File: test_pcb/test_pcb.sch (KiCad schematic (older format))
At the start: 19 parts, among them K0 KEYSW, K1 KEYSW, K2 KEYSW, K3 KEYSW, K5 KEYSW, U1 74HC595, U2 Teensy3.2

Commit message: updated test_pcb
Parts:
- added P1, P2: CONN_01X08, Pin_Headers:Pin_Header_Straight_1x08_Pitch2.00mm, symbol CONN_01X08
- added U2: 74HC595, Housings_SSOP:TSSOP-16_4.4x5mm_Pitch0.65mm, symbol 74HC595
- U0: renamed from U2; footprint Socket_Strips:Socket_Strip_Angled_2x27_Pitch2.54mm -> Teensy:Teensy30_31_32_LC
- U1: footprint SMD_Packages:SO-16-L -> Housings_SSOP:TSSOP-16_4.4x5mm_Pitch0.65mm
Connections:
- net labels added: GND, GND0, GND1, sr_clk0, sr_data0, sr_data1
- net labels removed: sr_data
- wire segments 46 -> 84
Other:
- moved on the sheet: D0, D1, D2, D3, D5, K0, K1, K2, K3, K5, U0

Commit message: test_pcb first pass complete
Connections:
- wire segments 84 -> 50
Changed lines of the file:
@@
 Text GLabel 8350 5050 0    60   Input ~ 0
 col1_sled_cath
+Text GLabel 8350 5750 0    60   Input ~ 0
+row0_sled_r
 Text GLabel 8350 5850 0    60   Input ~ 0
-row0_sled_r
+row0_sled_g
 Text GLabel 8350 5950 0    60   Input ~ 0
-row0_sled_g
+row0_sled_b
+Text GLabel 8350 6250 0    60   Input ~ 0
+row1_sled_r
+Text GLabel 8350 6150 0    60   Input ~ 0
+row1_sled_g
 Text GLabel 8350 6050 0    60   Input ~ 0
-row0_sled_b
-Text GLabel 8350 6150 0    60   Input ~ 0
-row1_sled_r
-Text GLabel 8350 6250 0    60   Input ~ 0
-row1_sled_g
-Text GLabel 8350 6350 0    60   Input ~ 0
 row1_sled_b
 Text GLabel 9750 5050 2    60   Input ~ 0
@@
 	4100 2150 4100 2200
 Wire Wire Line
-	2800 2400 3000 2400
-Wire Wire Line
-	3000 2400 4100 2400
-Wire Wire Line
-	4100 2400 5400 2400
-Wire Wire Line
-	2800 1900 3000 1900
-Wire Wire Line
-	3000 1900 4100 1900
+	2800 2400 5400 2400
+Wire Wire Line
+	2800 1900 4100 1900
 Connection ~ 3600 1650
 Connection ~ 4700 1650
@@
 Connection ~ 3000 2400
 Wire Wire Line
-	4800 3150 4800 3400
-Wire Wire Line
-	4800 3400 4800 3600
-Wire Wire Line
-	4800 3600 4800 3800
-Wire Wire Line
-	4800 3800 4800 4500
-Wire Wire Line
-	4800 4500 4800 4700
-Wire Wire Line
-	4800 4700 4800 4900
+	4800 3150 4800 4900
 Connection ~ 4800 4700
 Wire Wire Line
-	3000 3150 3000 3400
-Wire Wire Line
-	3000 3400 3000 3600
-Wire Wire Line
-	3000 3600 3000 3800
-Wire Wire Line
-	3000 3800 3000 4500
-Wire Wire Line
-	3000 4500 3000 4700
-Wire Wire Line
-	3000 4700 3000 4900
+	3000 3150 3000 4900
 Connection ~ 3000 4700
 Connection ~ 3000 3600
 Connection ~ 4800 3600
 Wire Wire Line
-	3600 4050 4500 4050
-Wire Wire Line
-	4500 4050 5400 4050
-Wire Wire Line
-	5400 4050 5500 4050
-Wire Wire Line
-	3500 4150 4400 4150
-Wire Wire Line
-	4400 4150 5300 4150
-Wire Wire Line
-	5300 4150 6100 4150
-Wire Wire Line
-	3400 4250 4300 4250
-Wire Wire Line
-	4300 4250 5200 4250
-Wire Wire Line
-	5200 4250 6100 4250
+	3600 4050 5500 4050
+Wire Wire Line
+	3500 4150 6100 4150
+Wire Wire Line
+	3400 4250 6100 4250
 Wire Wire Line
 	3400 3800 3400 4250
@@
 Connection ~ 5400 4050
 Wire Wire Line
-	3600 5150 4500 5150
-Wire Wire Line
-	4500 5150 5400 5150
-Wire Wire Line
-	5400 5150 5500 5150
-Wire Wire Line
-	3500 5250 4400 5250
-Wire Wire Line
-	4400 5250 5300 5250
-Wire Wire Line
-	5300 5250 6100 5250
-Wire Wire Line
-	3400 5350 4300 5350
-Wire Wire Line
-	4300 5350 5200 5350
-Wire Wire Line
-	5200 5350 6100 5350
+	3600 5150 5500 5150
+Wire Wire Line
+	3500 5250 6100 5250
+Wire Wire Line
+	3400 5350 6100 5350
 Wire Wire Line
 	5200 5350 5200 4900
@@
 Connection ~ 6000 1650
 Wire Wire Line
-	3900 3150 3900 3400
-Wire Wire Line
-	3900 3400 3900 3600
-Wire Wire Line
-	3900 3600 3900 3800
-Wire Wire Line
-	3900 3800 3900 4500
-Wire Wire Line
-	3900 4500 3900 4700
-Wire Wire Line
-	3900 4700 3900 4900
+	3900 3150 3900 4900
 Connection ~ 3900 4700
 Connection ~ 3900 3600
@@
 Connection ~ 6000 2150
 Wire Wire Line
-	6000 1650 6000 2150
-Wire Wire Line
-	6000 2150 6000 2500
-Wire Wire Line
-	4700 1650 4700 2150
-Wire Wire Line
-	4700 2150 4700 2500
-Wire Wire Line
-	3600 1650 3600 2150
-Wire Wire Line
-	3600 2150 3600 2500
+	6000 1650 6000 2500
+Wire Wire Line
+	4700 1650 4700 2500
+Wire Wire Line
+	3600 1650 3600 2500
 $Comp
 L 74HC595 U2
@@
 	10700 5850 10600 5850
 Wire Wire Line
-	10700 5650 10700 5750
-Wire Wire Line
-	10700 5750 10700 5850
+	10700 5650 10700 5850
 Wire Wire Line
 	10700 5650 10600 5650

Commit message: test_pcb small stuff
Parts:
- added P0: CONN_01X08, Connectors_Molex:Molex_PicoBlade_53261-0871_08x1.25mm_Angled, symbol CONN_01X08
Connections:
- net labels added: BTN0, BTN1, BTN2, DATA, TP_CLK, TP_RST, VCC
- net labels removed: GND0, GND1
- wire segments 50 -> 46
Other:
- moved on the sheet: D0, D1, D2, D3, D5, K0, K1, K2, K3, K5
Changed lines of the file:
@@
 L KEYSW K0
 U 1 1 5894086E
+P 3300 1150
+F 0 "K0" H 3250 1150 60  0000 C CNN
+F 1 "KEYSW" H 3300 1050 60  0001 C CNN
+F 2 "cherry_rgb:CHERRY_PLATE_NH_100H" H 3300 1150 60  0001 C CNN
+F 3 "" H 3300 1150 60  0000 C CNN
+	1    3300 1150
+	1    0    0    -1
+$EndComp
+$Comp
+L KEYSW K2
+U 1 1 58940BCD
+P 4400 1150
+F 0 "K2" H 4350 1150 60  0000 C CNN
+F 1 "KEYSW" H 4400 1050 60  0001 C CNN
+F 2 "cherry_rgb:CHERRY_PLATE_NH_100H" H 4400 1150 60  0001 C CNN
+F 3 "" H 4400 1150 60  0000 C CNN
+	1    4400 1150
+	1    0    0    -1
+$EndComp
+$Comp
+L KEYSW K1
+U 1 1 58940C88
 P 3300 1650
-F 0 "K0" H 3250 1650 60  0000 C CNN
+F 0 "K1" H 3250 1650 60  0000 C CNN
 F 1 "KEYSW" H 3300 1550 60  0001 C CNN
 F 2 "cherry_rgb:CHERRY_PLATE_NH_100H" H 3300 1650 60  0001 C CNN
@@
 $EndComp
 $Comp
-L KEYSW K2
-U 1 1 58940BCD
+L KEYSW K3
+U 1 1 58940C8E
 P 4400 1650
-F 0 "K2" H 4350 1650 60  0000 C CNN
+F 0 "K3" H 4350 1650 60  0000 C CNN
 F 1 "KEYSW" H 4400 1550 60  0001 C CNN
 F 2 "cherry_rgb:CHERRY_PLATE_NH_100H" H 4400 1650 60  0001 C CNN
@@
 $EndComp
 $Comp
-L KEYSW K1
-U 1 1 58940C88
-P 3300 2150
-F 0 "K1" H 3250 2150 60  0000 C CNN
-F 1 "KEYSW" H 3300 2050 60  0001 C CNN
-F 2 "cherry_rgb:CHERRY_PLATE_NH_100H" H 3300 2150 60  0001 C CNN
-F 3 "" H 3300 2150 60  0000 C CNN
-	1    3300 2150
-	1    0    0    -1
-$EndComp
-$Comp
-L KEYSW K3
-U 1 1 58940C8E
-P 4400 2150
-F 0 "K3" H 4350 2150 60  0000 C CNN
-F 1 "KEYSW" H 4400 2050 60  0001 C CNN
-F 2 "cherry_rgb:CHERRY_PLATE_NH_100H" H 4400 2150 60  0001 C CNN
-F 3 "" H 4400 2150 60  0000 C CNN
-	1    4400 2150
-	1    0    0    -1
-$EndComp
-$Comp
 L D D0
 U 1 1 58940C9B
+P 3000 1350
+F 0 "D0" V 2850 1300 60  0000 C CNN
+F 1 "D" V 3150 1300 60  0001 C CNN
+F 2 "Diodes_SMD:D_SOD-123" H 3000 1350 60  0001 C CNN
+F 3 "" H 3000 1350 60  0000 C CNN
+	1    3000 1350
+	-1   0    0    1
+$EndComp
+$Comp
+L D D2
+U 1 1 589410AE
+P 4100 1350
+F 0 "D2" V 3950 1300 60  0000 C CNN
+F 1 "D" V 4250 1300 60  0001 C CNN
+F 2 "Diodes_SMD:D_SOD-123" H 4100 1350 60  0001 C CNN
+F 3 "" H 4100 1350 60  0000 C CNN
+	1    4100 1350
+	-1   0    0    1
+$EndComp
+$Comp
+L D D1
+U 1 1 58941204
 P 3000 1850
-F 0 "D0" V 2850 1800 60  0000 C CNN
+F 0 "D1" V 2850 1800 60  0000 C CNN
 F 1 "D" V 3150 1800 60  0001 C CNN
 F 2 "Diodes_SMD:D_SOD-123" H 3000 1850 60  0001 C CNN
@@
 $EndComp
 $Comp
-L D D2
-U 1 1 589410AE
+L D D3
+U 1 1 5894120A
 P 4100 1850
-F 0 "D2" V 3950 1800 60  0000 C CNN
+F 0 "D3" V 3950 1800 60  0000 C CNN
 F 1 "D" V 4250 1800 60  0001 C CNN
 F 2 "Diodes_SMD:D_SOD-123" H 4100 1850 60  0001 C CNN
@@
 	-1   0    0    1
 $EndComp
-$Comp
-L D D1
-U 1 1 58941204
-P 3000 2350
-F 0 "D1" V 2850 2300 60  0000 C CNN
-F 1 "D" V 3150 2300 60  0001 C CNN
-F 2 "Diodes_SMD:D_SOD-123" H 3000 2350 60  0001 C CNN
-F 3 "" H 3000 2350 60  0000 C CNN
-	1    3000 2350
-	-1   0    0    1
-$EndComp
-$Comp
-L D D3
-U 1 1 5894120A
-P 4100 2350
-F 0 "D3" V 3950 2300 60  0000 C CNN
-F 1 "D" V 4250 2300 60  0001 C CNN
-F 2 "Diodes_SMD:D_SOD-123" H 4100 2350 60  0001 C CNN
-F 3 "" H 4100 2350 60  0000 C CNN
-	1    4100 2350
-	-1   0    0    1
-$EndComp
+Text GLabel 2800 1400 0    60   Input ~ 0
+row0
 Text GLabel 2800 1900 0    60   Input ~ 0
-row0
-Text GLabel 2800 2400 0    60   Input ~ 0
 row1
-Text GLabel 3600 2500 3    60   Input ~ 0
+Text GLabel 3600 2000 3    60   Input ~ 0
 col0
-Text GLabel 4700 2500 3    60   Input ~ 0
+Text GLabel 4700 2000 3    60   Input ~ 0
 col1
 Text GLabel 7000 2200 0    60   Input ~ 0
@@
 L KEYSW K5
 U 1 1 58950DFF
-P 5700 2150
-F 0 "K5" H 5650 2150 60  0000 C CNN
-F 1 "KEYSW" H 5700 2050 60  0001 C CNN
-F 2 "cherry_rgb:CHERRY_PLATE_NH_100H" H 5700 2150 60  0001 C CNN
-F 3 "" H 5700 2150 60  0000 C CNN
-	1    5700 2150
+P 5700 1650
+F 0 "K5" H 5650 1650 60  0000 C CNN
+F 1 "KEYSW" H 5700 1550 60  0001 C CNN
+F 2 "cherry_rgb:CHERRY_PLATE_NH_100H" H 5700 1650 60  0001 C CNN
+F 3 "" H 5700 1650 60  0000 C CNN
+	1    5700 1650
 	1    0    0    -1
 $EndComp
@@
 L D D5
 U 1 1 58950E0B
-P 5400 2350
-F 0 "D5" V 5250 2300 60  0000 C CNN
-F 1 "D" V 5550 2300 60  0001 C CNN
-F 2 "Diodes_SMD:D_SOD-123" H 5400 2350 60  0001 C CNN
-F 3 "" H 5400 2350 60  0000 C CNN
-	1    5400 2350
-	-1   0    0    1
-$EndComp
-Text GLabel 6000 2500 3    60   Input ~ 0
+P 5400 1850
+F 0 "D5" V 5250 1800 60  0000 C CNN
+F 1 "D" V 5550 1800 60  0001 C CNN
+F 2 "Diodes_SMD:D_SOD-123" H 5400 1850 60  0001 C CNN
+F 3 "" H 5400 1850 60  0000 C CNN
+	1    5400 1850
+	-1   0    0    1
+$EndComp
+Text GLabel 6000 2000 3    60   Input ~ 0
 col2
 $Comp
@@
 	1    0    0    -1
 $EndComp
+$Comp
+L 74HC595 U2
+U 1 1 58957349
+P 9050 5900
+F 0 "U2" H 9200 6500 50  0000 C CNN
+F 1 "74HC595" H 9050 5300 50  0000 C CNN
+F 2 "Housings_SSOP:TSSOP-16_4.4x5mm_Pitch0.65mm" H 9050 5900 50  0001 C CNN
+F 3 "" H 9050 5900 50  0000 C CNN
+	1    9050 5900
+	-1   0    0    1
+$EndComp
+Text GLabel 9750 6350 2    60   Input ~ 0
+sr_data1
+Text GLabel 10650 5300 0    60   Input ~ 0
+sr_data1
+$Comp
+L CONN_01X08 P1
+U 1 1 58957DB2
+P 10850 4950
+F 0 "P1" H 10850 5400 50  0000 C CNN
+F 1 "CONN_01X08" V 10950 4950 50  0000 C CNN
+F 2 "Pin_Headers:Pin_Header_Straight_1x08_Pitch2.00mm" H 10850 4950 50  0001 C CNN
+F 3 "" H 10850 4950 50  0000 C CNN
+	1    10850 4950
+	1    0    0    -1
+$EndComp
+Text GLabel 10650 4600 0    60   Input ~ 0
+sr_clk0
+Text GLabel 9750 4850 2    60   Input ~ 0
+sr_clk0
+Text GLabel 9750 6150 2    60   Input ~ 0
+sr_clk0
+Text GLabel 10650 4900 0    60   Input ~ 0
+GND
+Text GLabel 9750 4450 2    60   Input ~ 0
+GND
+Text GLabel 9750 5750 2    60   Input ~ 0
+GND
+Text GLabel 10650 5000 0    60   Input ~ 0
+VCC
+$Comp
+L CONN_01X08 P0
+U 1 1 5897F60A
+P 7600 3600
+F 0 "P0" H 7600 4050 50  0000 C CNN
+F 1 "CONN_01X08" V 7700 3600 50  0000 C CNN
+F 2 "Connectors_Molex:Molex_PicoBlade_53261-0871_08x1.25mm_Angled" H 7600 3600 50  0001 C CNN
+F 3 "" H 7600 3600 50  0000 C CNN
+	1    7600 3600
+	1    0    0    -1
+$EndComp
+Text GLabel 7400 3950 0    60   Input ~ 0
+BTN0
+Text GLabel 7400 3850 0    60   Input ~ 0
+BTN1
+Text GLabel 7400 3750 0    60   Input ~ 0
+BTN2
+Text GLabel 7400 3650 0    60   Input ~ 0
+VCC
+Text GLabel 7400 3250 0    60   Input ~ 0
+GND
+Text GLabel 7400 3350 0    60   Input ~ 0
+DATA
+Text GLabel 7400 3550 0    60   Input ~ 0
+TP_RST
+Text GLabel 7400 3450 0    60   Input ~ 0
+TP_CLK
+Wire Wire Line
+	3000 1150 3000 1200
+Wire Wire Line
+	4100 1150 4100 1200
 Wire Wire Line
 	3000 1650 3000 1700
@@
 	4100 1650 4100 1700
 Wire Wire Line
-	3000 2150 3000 2200
-Wire Wire Line
-	4100 2150 4100 2200
-Wire Wire Line
-	2800 2400 5400 2400
-Wire Wire Line
-	2800 1900 4100 1900
-Connection ~ 3600 1650
-Connection ~ 4700 1650
+	2800 1900 5400 1900
+Wire Wire Line
+	2800 1400 4100 1400
+Connection ~ 3600 1150
+Connection ~ 4700 1150
+Connection ~ 3000 1400
 Connection ~ 3000 1900
-Connection ~ 3000 2400
 Wire Wire Line
 	4800 3150 4800 4900
@@
 	6000 5150 6100 5150
 Wire Wire Line
-	5400 2150 5400 2200
-Connection ~ 6000 1650
+	5400 1650 5400 1700
+Connection ~ 6000 1150
 Wire Wire Line
 	3900 3150 3900 4900
@@
 Connection ~ 4400 5250
 Connection ~ 4300 5350
-Connection ~ 4100 2400
-Connection ~ 3600 2150
-Connection ~ 4700 2150
-Connection ~ 6000 2150
-Wire Wire Line
-	6000 1650 6000 2500
-Wire Wire Line
-	4700 1650 4700 2500
-Wire Wire Line
-	3600 1650 3600 2500
-$Comp
-L 74HC595 U2
-U 1 1 58957349
-P 9050 5900
-F 0 "U2" H 9200 6500 50  0000 C CNN
-F 1 "74HC595" H 9050 5300 50  0000 C CNN
-F 2 "Housings_SSOP:TSSOP-16_4.4x5mm_Pitch0.65mm" H 9050 5900 50  0001 C CNN
-F 3 "" H 9050 5900 50  0000 C CNN
-	1    9050 5900
-	-1   0    0    1
-$EndComp
-Text GLabel 9750 6350 2    60   Input ~ 0
-sr_data1
-Text GLabel 10650 5300 0    60   Input ~ 0
-sr_data1
-$Comp
-L CONN_01X08 P1
-U 1 1 58957DB2
-P 10850 4950
-F 0 "P1" H 10850 5400 50  0000 C CNN
-F 1 "CONN_01X08" V 10950 4950 50  0000 C CNN
-F 2 "Pin_Headers:Pin_Header_Straight_1x08_Pitch2.00mm" H 10850 4950 50  0001 C CNN
-F 3 "" H 10850 4950 50  0000 C CNN
-	1    10850 4950
-	1    0    0    -1
-$EndComp
-Text GLabel 10650 4600 0    60   Input ~ 0
-sr_clk0
-Text GLabel 9750 4850 2    60   Input ~ 0
-sr_clk0
-Text GLabel 9750 6150 2    60   Input ~ 0
-sr_clk0
-Text GLabel 10650 4900 0    60   Input ~ 0
-GND
-Text GLabel 9750 4450 2    60   Input ~ 0
-GND0
-Text GLabel 9750 5750 2    60   Input ~ 0
-GND1
-Text GLabel 10800 5750 2    60   Input ~ 0
-GND
-Text GLabel 10600 5850 0    60   Input ~ 0
-GND1
-Text GLabel 10600 5650 0    60   Input ~ 0
-GND0
-Wire Wire Line
-	10700 5850 10600 5850
-Wire Wire Line
-	10700 5650 10700 5850
-Wire Wire Line
-	10700 5650 10600 5650
-Wire Wire Line
-	10700 5750 10800 5750
-Connection ~ 10700 5750
+Connection ~ 4100 1900
+Connection ~ 3600 1650
+Connection ~ 4700 1650
+Connection ~ 6000 1650
+Wire Wire Line
+	6000 1150 6000 2000
+Wire Wire Line
+	4700 1150 4700 2000
+Wire Wire Line
+	3600 1150 3600 2000
 $EndSCHEMATC

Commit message: test is now a numpad for led testing + a 6 key test for the trackpoint
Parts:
- removed P1, P2: CONN_01X08, Pin_Headers:Pin_Header_Straight_1x08_Pitch2.00mm, symbol CONN_01X08
- removed R1, R2: R, Resistors_SMD:R_0402, symbol R
- removed SMDLED0, SMDLED1, SMDLED2, SMDLED3, SMDLED5: LED_RGB, cherry_rgb:SMLVN6RGB, symbol LED_RGB
- removed U1, U2: 74HC595, Housings_SSOP:TSSOP-16_4.4x5mm_Pitch0.65mm, symbol 74HC595
- added D10, D12, D13, D14, D15, D16, D17, D18, D20, D21, D22, D24, D25, D26, D27, D4, D6, D7, D8, D9: D, Diodes_SMD:D_SOD-123, symbol D
- added K10, K12, K13, K14, K16, K17, K18, K21, K24, K25, K26, K27, K6, K8, K9: KEYSW, cherry_rgb:CHERRY_PLATE_NH_100H, symbol KEYSW
- added K15, K7: KEYSW, cherry_rgb:CHERRY_PLATE_150V, symbol KEYSW
- added K20: KEYSW, cherry_rgb:CHERRY_PLATE_200H, symbol KEYSW
- added K22: KEYSW, cherry_rgb:CHERRY_PLATE_200V, symbol KEYSW
- added K4: KEYSW, cherry_rgb:CHERRY_PLATE_91.6H, symbol KEYSW
- added R3, R4, R5: R, Resistors_SMD:R_0603_HandSoldering, symbol R
- added SMD_LED1, SMD_LED10, SMD_LED11, SMD_LED12, SMD_LED13, SMD_LED14, SMD_LED15, SMD_LED16, SMD_LED17, SMD_LED18, SMD_LED19, SMD_LED2, SMD_LED20, SMD_LED21, SMD_LED3, SMD_LED4, SMD_LED5, SMD_LED6, SMD_LED7, SMD_LED8, SMD_LED9: SMLVN6RGB, cherry_rgb:SMLVN6RGB, symbol SMLVN6RGB
- added U3: STP16CP05, symbol STP16CP05
- K0, K1, K2, K3: footprint cherry_rgb:CHERRY_PLATE_NH_100H -> cherry_rgb:CHERRY_PLATE_91.6H
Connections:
- net labels added: a0, a1, a2, a3, a4, a5, a6, blue0, blue1, blue2, c0, c1, c2, c3, green0, green1, green2, r0, r1, r2, r3, r4, r5, red0, red1, red2
- net labels removed: col0, col0_sled_cath, col1, col1_sled_cath, col2, col2_sled_cath, row0, row0_sled_b, row0_sled_g, row0_sled_r, row1, row1_sled_b, row1_sled_g, row1_sled_r, sr_clk0, sr_data0, sr_data1
- wire segments 46 -> 185
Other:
- moved on the sheet: P0, U0

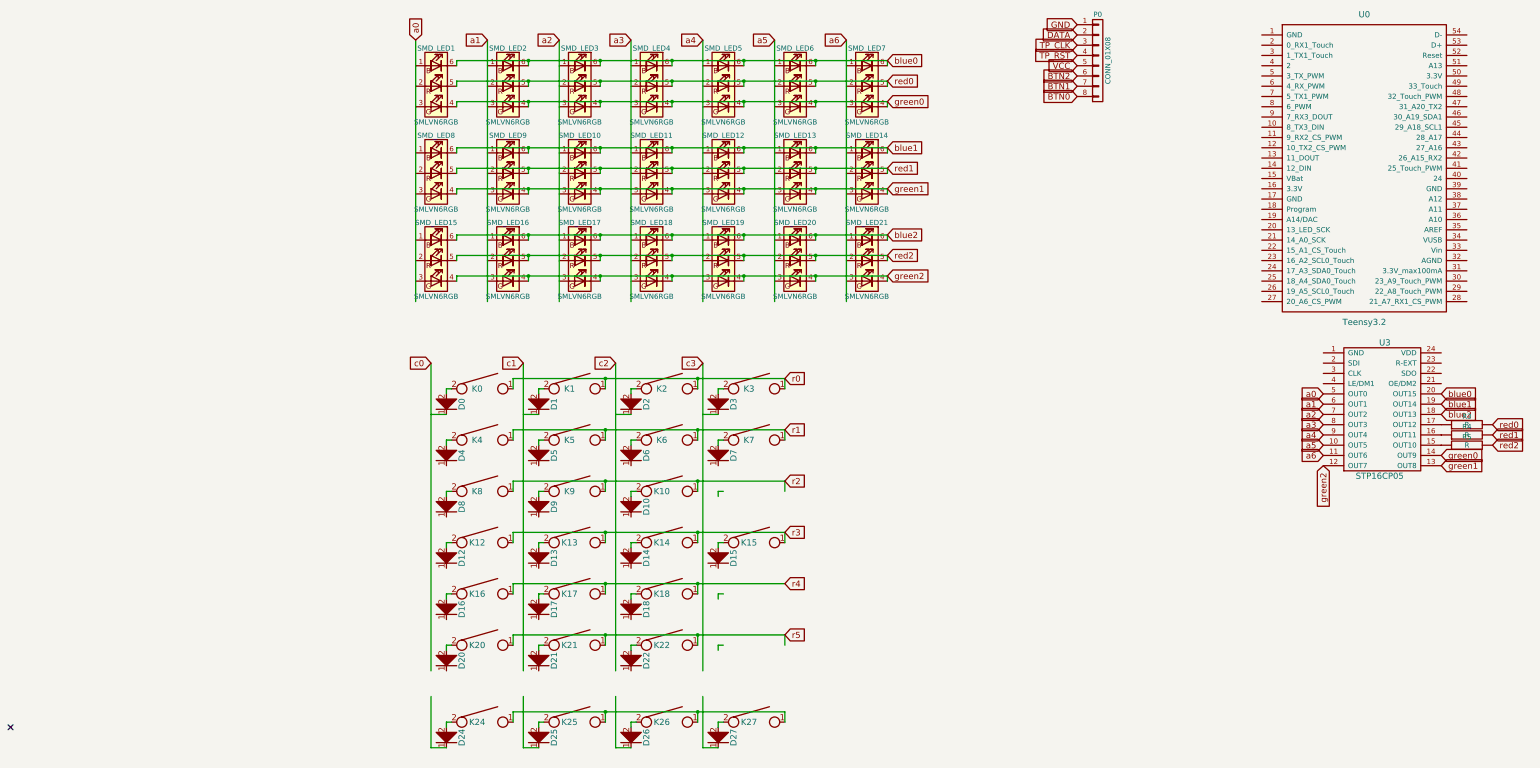
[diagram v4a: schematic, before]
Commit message: lots of progress on numpad
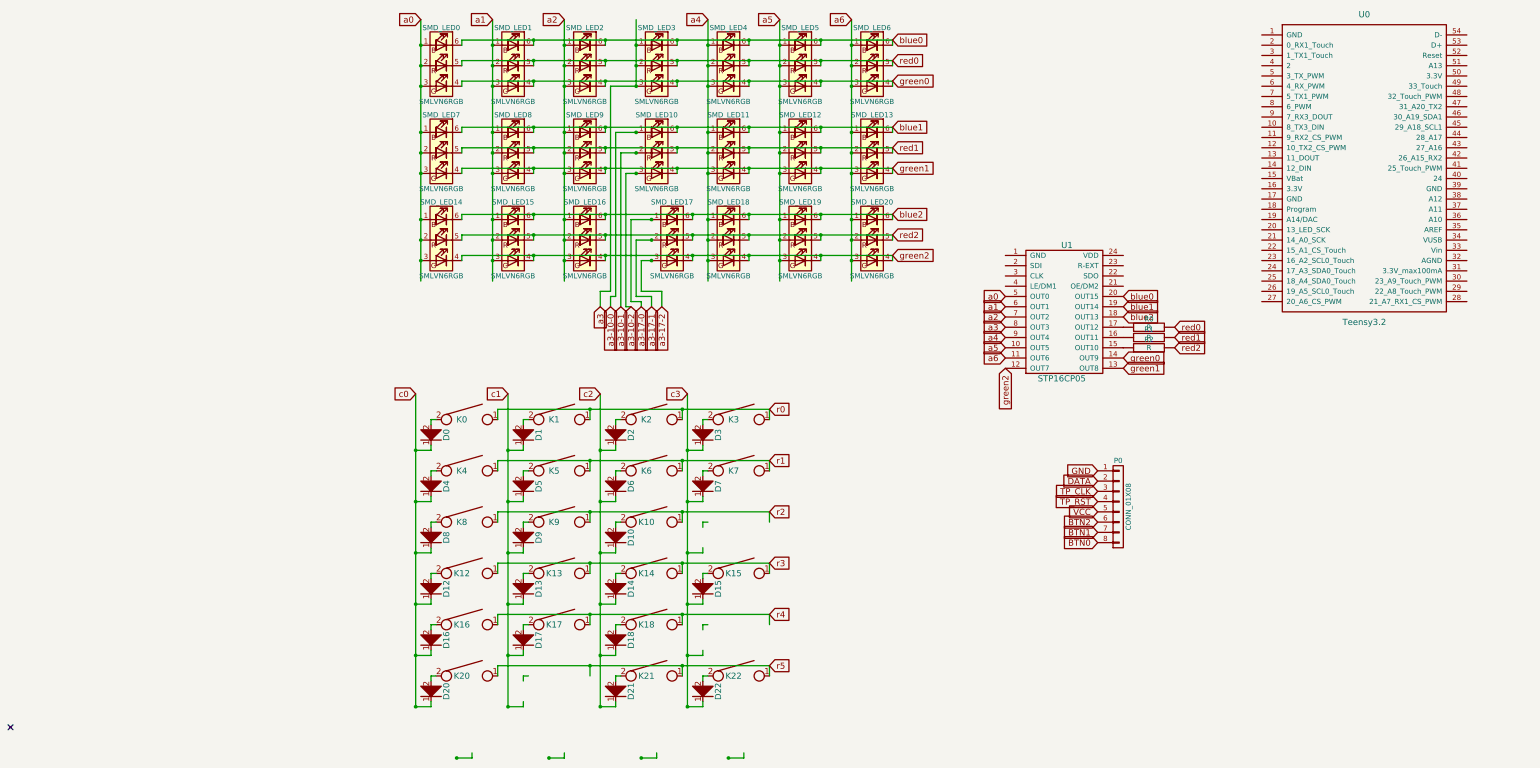
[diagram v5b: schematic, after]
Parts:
- removed D24, D25, D26, D27: D, Diodes_SMD:D_SOD-123, symbol D
- removed K24, K25, K26, K27: KEYSW, cherry_rgb:CHERRY_PLATE_NH_100H, symbol KEYSW
- K4: footprint cherry_rgb:CHERRY_PLATE_91.6H -> cherry_rgb:CHERRY_PLATE_NH_100H
- U1: renamed from U3; footprint (none) -> Housings_SSOP:TSSOP-24_4.4x7.8mm_Pitch0.65mm
- renumbered R3 to R0, R4 to R1, R5 to R2, SMD_LED1 to SMD_LED0, SMD_LED2 to SMD_LED1, SMD_LED11 to SMD_LED10, SMD_LED12 to SMD_LED11, SMD_LED13 to SMD_LED12, SMD_LED14 to SMD_LED13, SMD_LED15 to SMD_LED14, SMD_LED16 to SMD_LED15, SMD_LED17 to SMD_LED16, SMD_LED18 to SMD_LED17, SMD_LED19 to SMD_LED18, SMD_LED20 to SMD_LED19, SMD_LED3 to SMD_LED2, SMD_LED21 to SMD_LED20, SMD_LED4 to SMD_LED3, SMD_LED5 to SMD_LED4, SMD_LED6 to SMD_LED5, SMD_LED7 to SMD_LED6, SMD_LED8 to SMD_LED7, SMD_LED9 to SMD_LED8, SMD_LED10 to SMD_LED9
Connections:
- net labels added: a3-10-0, a3-10-1, a3-10-2, a3-17-0, a3-17-1, a3-17-2
- wire segments 185 -> 375
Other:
- moved on the sheet: D0, D1, D10, D12, D13, D14, D15, D16, D17, D18, D2, D20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
